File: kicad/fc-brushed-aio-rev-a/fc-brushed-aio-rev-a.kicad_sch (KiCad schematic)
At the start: 51 parts, among them J1 Battery, J10 USART1, J11 USART2, J12 FC-ESC con, J13 Motors2, J14 UART4, J15 USART6, Q1 PMOS, SW1 SW_SPST, U1 STM32F405RGTx, U13 W25Q128JVS, U14 INA180A3, U2 BMP388, U3 BMI270, U4 TPS62172DSG, U5 GT-USB-7010AN, Y1 8 MHz

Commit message: More progress on pcb!
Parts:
- added J16, J17, J18: I2C, custom:Conn_4_Accesory, symbol Connector_Generic:Conn_01x04
- added J19: Debug, Connector_PinHeader_1.27mm:PinHeader_1x03_P1.27mm_Vertical, symbol Connector_Generic:Conn_01x03
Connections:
- net Current is gone; now on net CURR_EXT: J12.3 (Pin_3)
- net +3V3: now also J16.3 (Pin_3)
- net GND: now also J16.4 (Pin_4), J17.4 (Pin_4), J18.4 (Pin_4), J19.3 (Pin_3)
- net I2C1_SCL: now also J16.2 (Pin_2)
- net I2C1_SDA: now also J16.1 (Pin_1)
- net RX2: now also J15.2 (Pin_2); no longer J11.2 (Pin_2)
- net RX6: now also J11.2 (Pin_2); no longer J15.2 (Pin_2)
- net SWCLK: now also J19.2 (Pin_2)
- net SWDIO: now also J19.1 (Pin_1)
- net TX2: now also J15.1 (Pin_1); no longer J11.1 (Pin_1)
- net TX6: now also J11.1 (Pin_1); no longer J15.1 (Pin_1)
- net VBAT: now also J17.3 (Pin_3), J18.3 (Pin_3)
- net RGB_LED: now reaches U1.35 (PB14)
- net RGB_LED: now also J17.2 (Pin_2)
- net SERVO_1: now reaches U1.41 (PA8)
- net SERVO_1: now also J17.1 (Pin_1)
- net SERVO_2: now reaches U1.50 (PA15)
- net SERVO_2: now also J18.2 (Pin_2)
- net SERVO_3: now reaches U1.55 (PB3)
- net SERVO_3: now also J18.1 (Pin_1)
- net CURR_EXT: now reaches U1.8 (PC0)

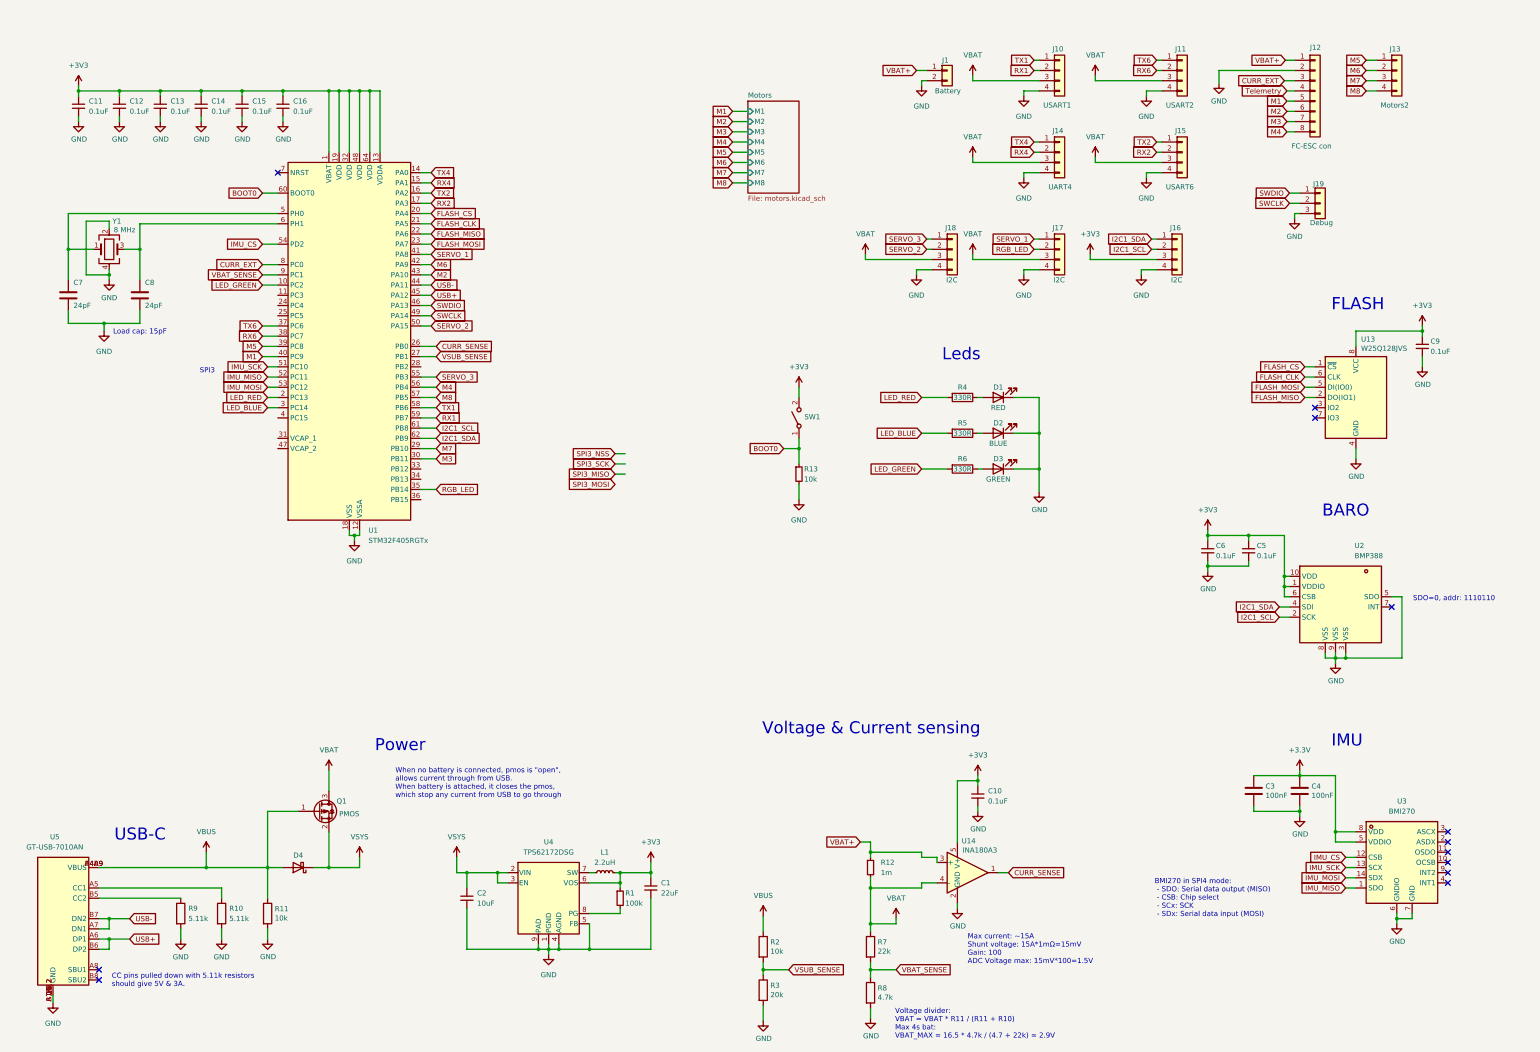
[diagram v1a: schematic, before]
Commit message: Majority of routing complete. Schematic too.
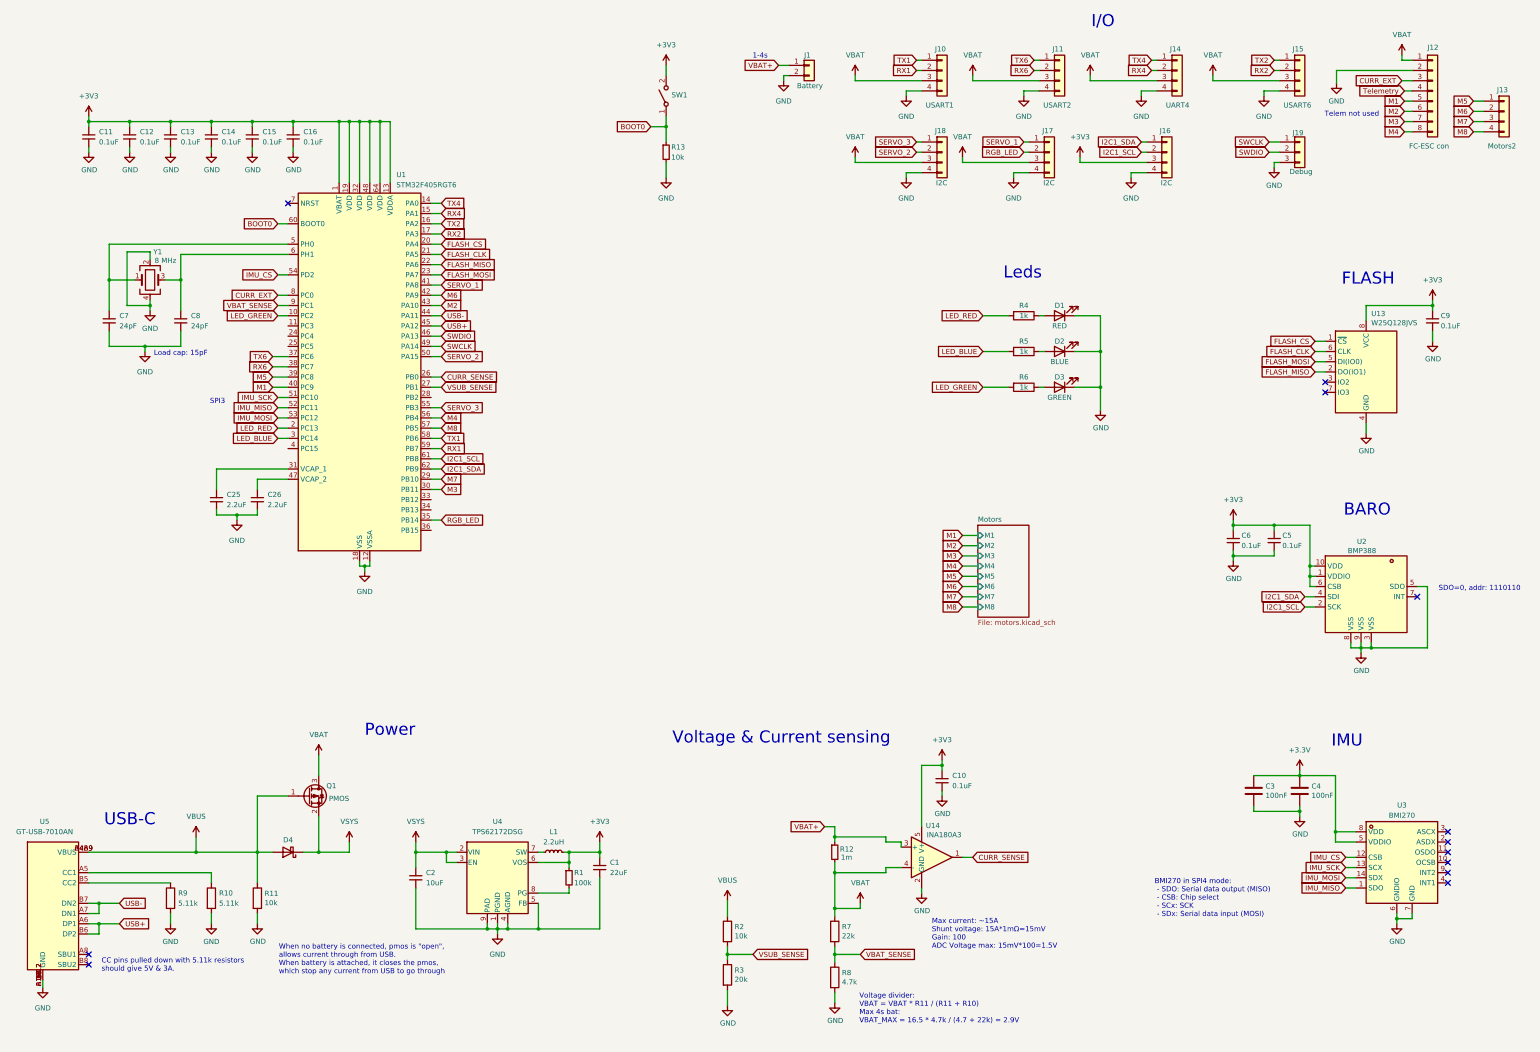
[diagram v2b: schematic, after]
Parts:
- removed C7, C8: 24pF, custom:C_0402_1005Metric_NoSilk, symbol Device:C
- added C25, C26: 2.2uF, custom:C_0402_1005Metric_NoSilk, symbol Device:C_Small
- added C7, C8: 24pF, custom:C_0402_1005Metric_NoSilk, symbol Device:C_Small
- R4, R5, R6: value 330R -> 1k
- U1: value STM32F405RGTx -> STM32F405RGT6
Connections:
- net GND: now also C25.2, C26.2, C7.2, C8.2
- net SWCLK: now also J19.1 (Pin_1); no longer J19.2 (Pin_2)
- net SWDIO: now also J19.2 (Pin_2); no longer J19.1 (Pin_1)
- net VBAT: now also J12.1 (Pin_1)
- net VBAT+: no longer J12.1 (Pin_1)
- net at U1.5 (PH0), Y1.1: now also C7.1
- net at U1.6 (PH1), Y1.3: now also C8.1
- net at U1.31 (VCAP_1): now also C25.1
- net at U1.47 (VCAP_2): now also C26.1
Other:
- note added: "1-4s"
- note added: "I/O"
- note added: "Telem not used"
- moved on the sheet: C1, C10, C11, C12, C13, C14, C15, C16, C2, C5, C6, C9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

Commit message: Got `hwdet.dat` file mostly complete. Can compile everything now
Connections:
- net M6: now also U1.41 (PA8); no longer U1.42 (PA9)
- net RGB_LED: now also J18.1 (Pin_1), U1.55 (PB3); no longer J17.2 (Pin_2), U1.35 (PB14)
- net SERVO_1: now also J17.2 (Pin_2), U1.35 (PB14); no longer J17.1 (Pin_1), U1.41 (PA8)
- net SERVO_2: now also J17.1 (Pin_1), U1.36 (PB15); no longer J18.2 (Pin_2), U1.50 (PA15)
- net SERVO_3: now also J18.2 (Pin_2), U1.50 (PA15); no longer J18.1 (Pin_1), U1.55 (PB3)
- net VSUB_SENSE: now also U1.42 (PA9); no longer U1.27 (PB1)
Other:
- note added: "SPI1"
- moved on the sheet: D1, D2, D3, R4, R5, R6

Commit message: Almost done with pcb! Need final checks and some silkscreen design stuff
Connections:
- net +3V3 is gone; now on net +3.3V: C1.1, C10.1, C11.1, C12.1, C13.1, C14.1, C15.1, C16.1, C5.1, C6.1, C9.1, J16.3 (Pin_3), L1.2, R1.1, SW1.2 (B), U1.1 (VBAT), U1.13 (VDDA), U1.19 (VDD), U1.32 (VDD), U1.48 (VDD), U1.64 (VDD), U13.8 (VCC), U14.5 (V+), U2.1 (VDDIO), U2.10 (VDD), U2.6 (CSB), U4.6 (VOS)
- no-connect marks 12 -> 20
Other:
- note added: "16MB"
- note added: "Bootloader button"
- note added: "LEDs"
- note added: "MCU"
- note added: "MOTORS"
- note removed: "Leds"
- moved on the sheet: C5, C6, C9, J1, J10, J11, J12, J13, J14, J15, J16, J17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
